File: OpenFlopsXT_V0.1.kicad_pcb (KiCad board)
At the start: 2 copper layers, 83.9 x 68.6 mm, 77 parts, among them J1 UP, J2 DN, J3 R, J4 G, J5 FH12-24S-0.5SH(55), J6 OSHW_LOGO, P1 FLOPPY_CONN, P2 POWER_INPUT, P3 POWER_PASSTHRU, P4 PROG_PORT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

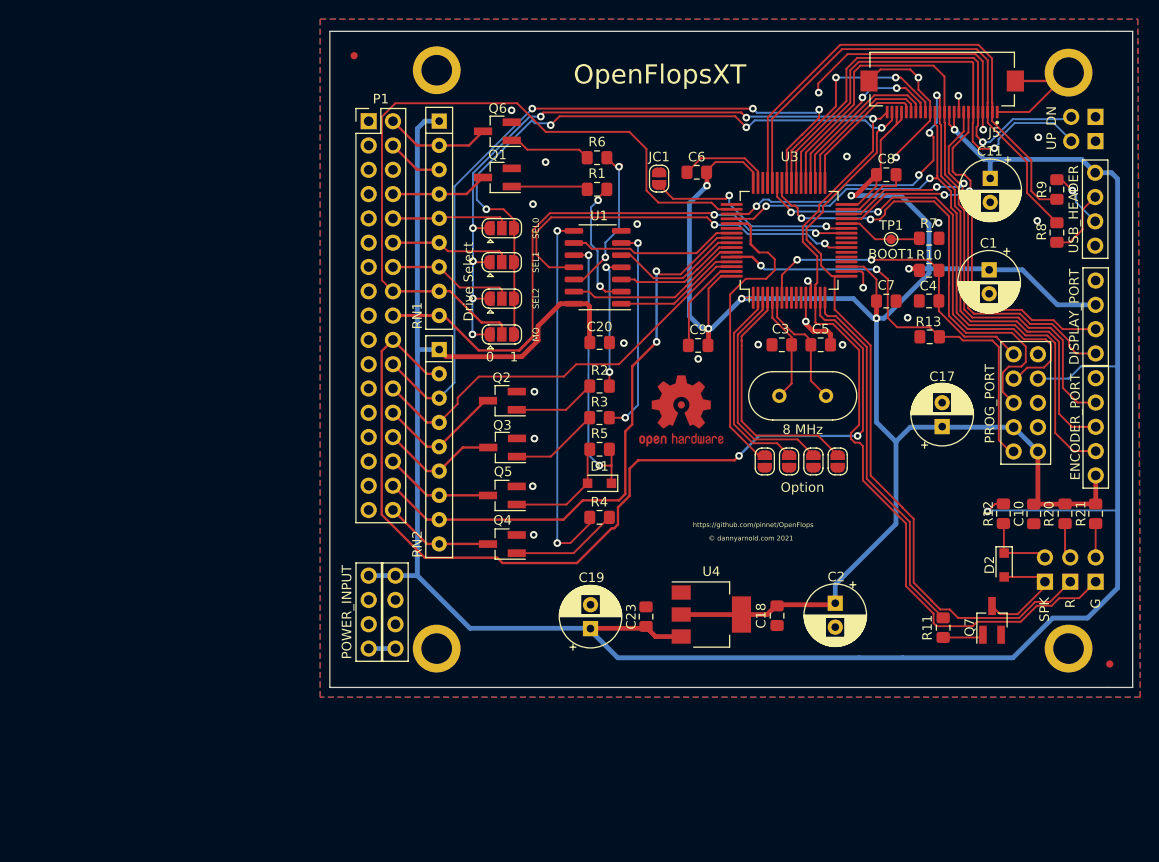
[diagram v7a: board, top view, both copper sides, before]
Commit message: Cleanup and fix silkscreen isue. OpenFlopsXT
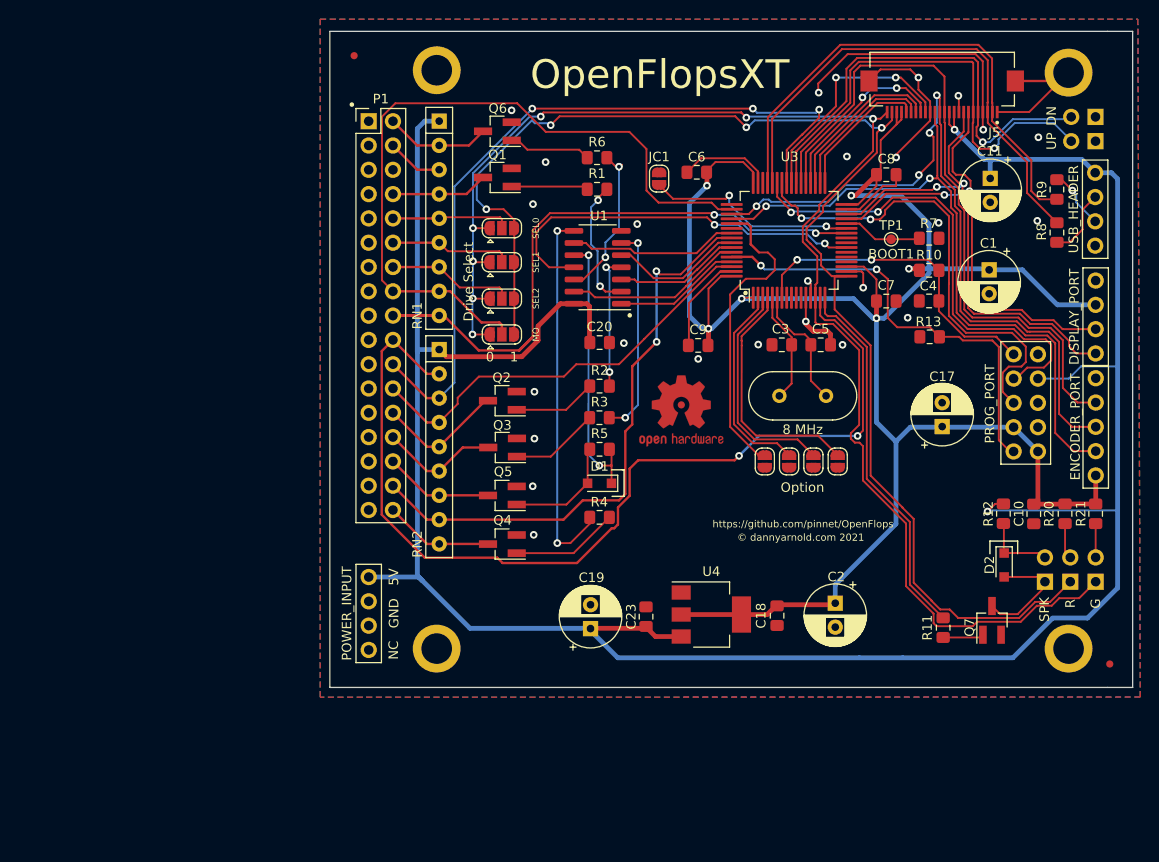
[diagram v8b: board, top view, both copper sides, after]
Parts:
- removed P3: POWER_PASSTHRU, OpenFlops:PinHeader_1x04_P2.54mm_Vertical_Power
- moved P2 0.14 mm to (111.7, 118.0)
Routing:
- net unconnected-(P2-Pad4): track 2.79 -> 0.00 mm
- net +5V: track 262.6 -> 263.2 mm
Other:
- board text added: "5V"
- board text added: "GND"
- board text added: "NC"
